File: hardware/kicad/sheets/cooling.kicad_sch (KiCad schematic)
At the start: 22 parts, among them J10 ALPHACOOL ES FLOW (3-pin), J11 ALPHACOOL ES NTC 10k, J8 FAN (4-pin PWM), J9 PUMP (4-pin PWM), U21 EMC2303-x-KP

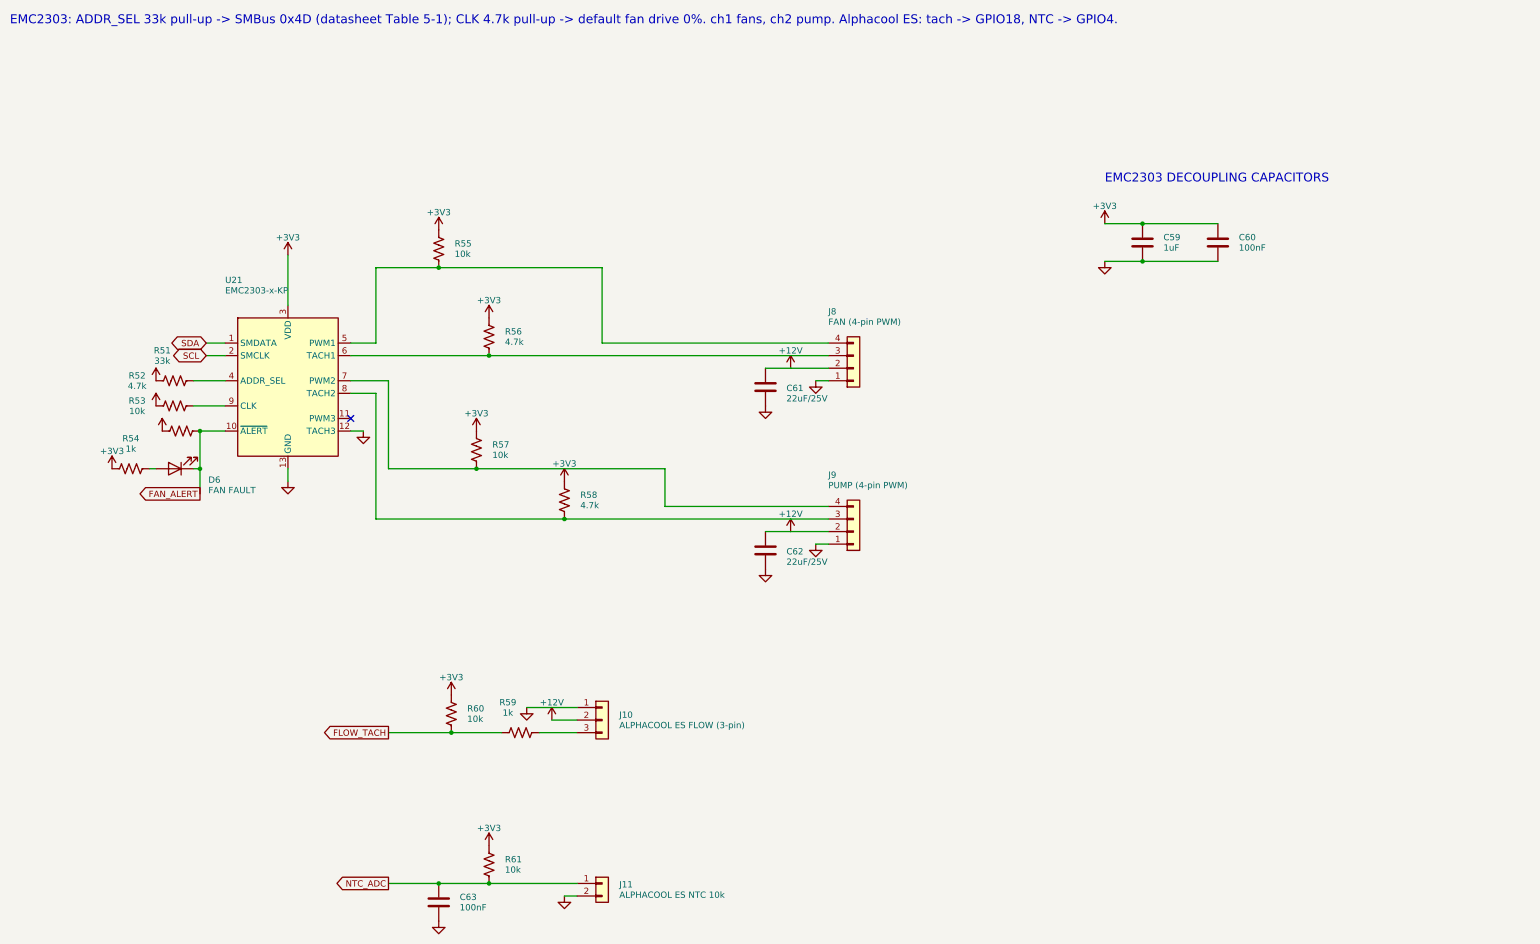
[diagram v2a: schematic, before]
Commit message: Fixing the UUID issues
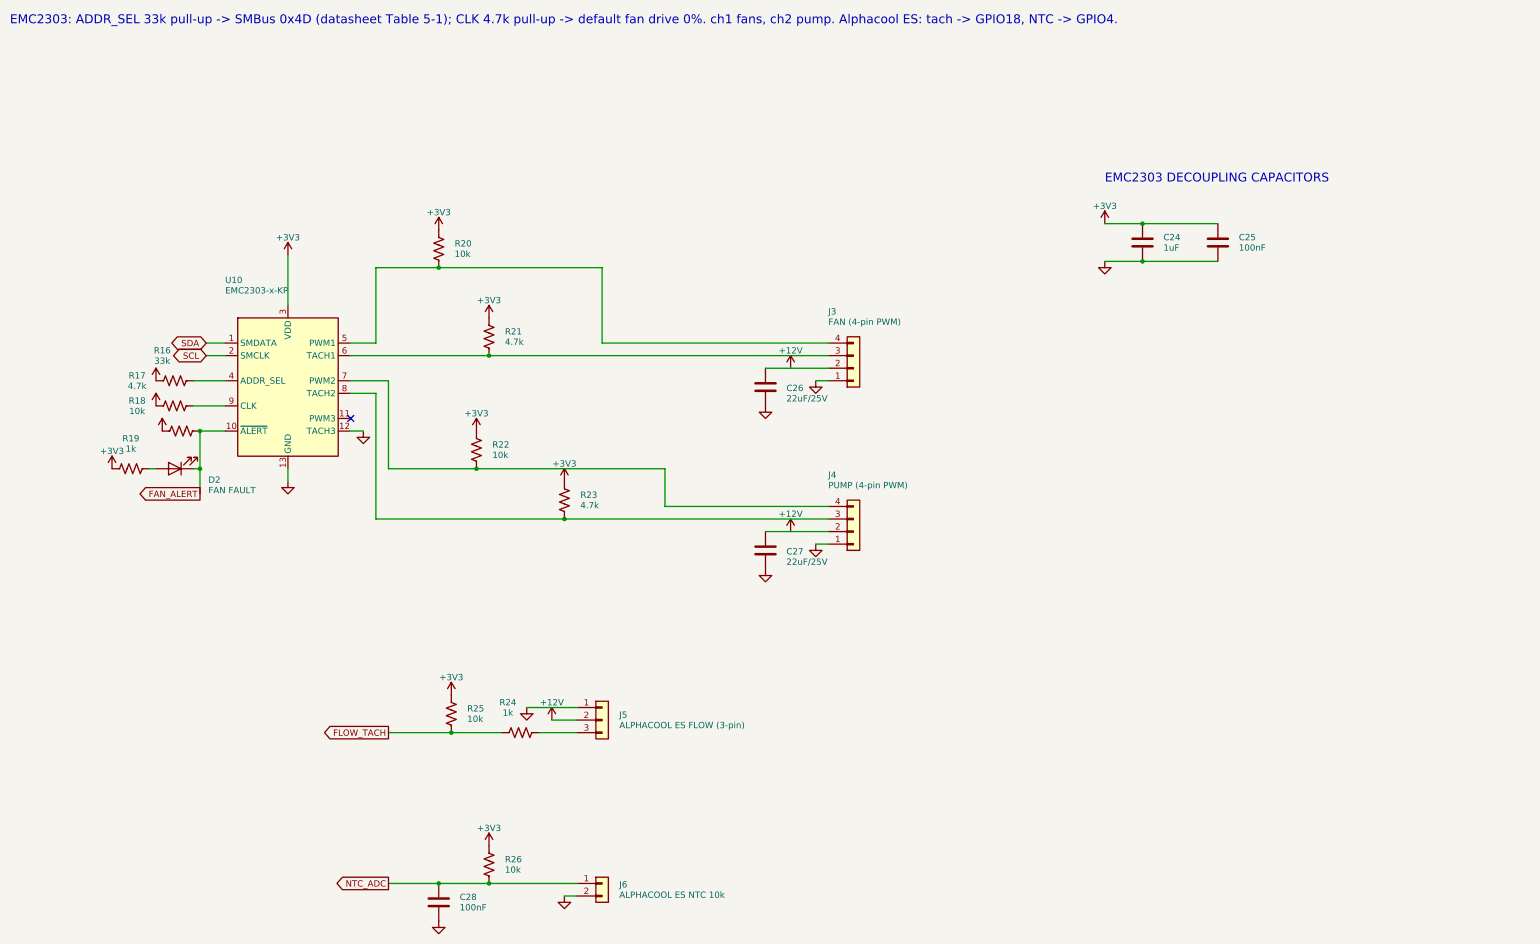
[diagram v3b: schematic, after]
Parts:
- removed C59: 1uF, Capacitor_SMD:C_0805_2012Metric, symbol Device:C
- removed C60, C63: 100nF, Capacitor_SMD:C_0603_1608Metric, symbol Device:C
- removed C61, C62: 22uF/25V, Capacitor_SMD:C_1210_3225Metric, symbol Device:C
- removed D6: FAN FAULT, LED_SMD:LED_0603_1608Metric, symbol Device:LED
- removed J10: ALPHACOOL ES FLOW (3-pin), Connector_Molex:Molex_KK-254_AE-6410-03A_1x03_P2.54mm_Vertical, symbol Connector_Generic:Conn_01x03
- removed J11: ALPHACOOL ES NTC 10k, Connector_JST:JST_XH_B2B-XH-A_1x02_P2.50mm_Vertical, symbol Connector_Generic:Conn_01x02
- removed J8: FAN (4-pin PWM), Connector_Molex:Molex_KK-254_AE-6410-04A_1x04_P2.54mm_Vertical, symbol Connector_Generic:Conn_01x04
- removed J9: PUMP (4-pin PWM), Connector_Molex:Molex_KK-254_AE-6410-04A_1x04_P2.54mm_Vertical, symbol Connector_Generic:Conn_01x04
- removed R51: 33k, Resistor_SMD:R_0603_1608Metric, symbol Device:R_US
- removed R52, R56, R58: 4.7k, Resistor_SMD:R_0603_1608Metric, symbol Device:R_US
- removed R53, R55, R57, R60, R61: 10k, Resistor_SMD:R_0603_1608Metric, symbol Device:R_US
- removed R54, R59: 1k, Resistor_SMD:R_0603_1608Metric, symbol Device:R_US
- removed U21: EMC2303-x-KP, Package_DFN_QFN:VQFN-12-1EP_4x4mm_P0.8mm_EP2.1x2.1mm_ThermalVias, symbol Driver_Motor:EMC2303-x-KP
- added C24: 1uF, Capacitor_SMD:C_0805_2012Metric, symbol Device:C
- added C25, C28: 100nF, Capacitor_SMD:C_0603_1608Metric, symbol Device:C
- added C26, C27: 22uF/25V, Capacitor_SMD:C_1210_3225Metric, symbol Device:C
- added D2: FAN FAULT, LED_SMD:LED_0603_1608Metric, symbol Device:LED
- added J3: FAN (4-pin PWM), Connector_Molex:Molex_KK-254_AE-6410-04A_1x04_P2.54mm_Vertical, symbol Connector_Generic:Conn_01x04
- added J4: PUMP (4-pin PWM), Connector_Molex:Molex_KK-254_AE-6410-04A_1x04_P2.54mm_Vertical, symbol Connector_Generic:Conn_01x04
- added J5: ALPHACOOL ES FLOW (3-pin), Connector_Molex:Molex_KK-254_AE-6410-03A_1x03_P2.54mm_Vertical, symbol Connector_Generic:Conn_01x03
- added J6: ALPHACOOL ES NTC 10k, Connector_JST:JST_XH_B2B-XH-A_1x02_P2.50mm_Vertical, symbol Connector_Generic:Conn_01x02
- added R16: 33k, Resistor_SMD:R_0603_1608Metric, symbol Device:R_US
- added R17, R21, R23: 4.7k, Resistor_SMD:R_0603_1608Metric, symbol Device:R_US
- added R18, R20, R22, R25, R26: 10k, Resistor_SMD:R_0603_1608Metric, symbol Device:R_US
- added R19, R24: 1k, Resistor_SMD:R_0603_1608Metric, symbol Device:R_US
- added U10: EMC2303-x-KP, Package_DFN_QFN:VQFN-12-1EP_4x4mm_P0.8mm_EP2.1x2.1mm_ThermalVias, symbol Driver_Motor:EMC2303-x-KP
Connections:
- net +12V: now also C26.1, C27.1, J3.2 (Pin_2), J4.2 (Pin_2), J5.2 (Pin_2)
- net +3V3: now also C24.1, C25.1, R16.1, R17.1, R18.1, R19.1, R20.1, R21.1, R22.1, R23.1, R25.1, R26.1, U10.3 (VDD)
- net FAN_ALERT: now also D2.1 (K), R18.2, U10.10 (~{ALERT})
- net FLOW_TACH: now also R24.1, R25.2
- net GND: now also C24.2, C25.2, C26.2, C27.2, C28.2, J3.1 (Pin_1), J4.1 (Pin_1), J5.1 (Pin_1), J6.2 (Pin_2), U10.12 (TACH3), U10.13 (GND)
- net NTC_ADC: now also C28.1, J6.1 (Pin_1), R26.2
- net SCL: now also U10.2 (SMCLK)
- net SDA: now also U10.1 (SMDATA)
- new net: J5.3 (Pin_3), R24.2
- new net: J3.4 (Pin_4), R20.2, U10.5 (PWM1)
- new net: D2.2 (A), R19.2
- new net: R16.2, U10.4 (ADDR_SEL)
- new net: J3.3 (Pin_3), R21.2, U10.6 (TACH1)
- new net: J4.4 (Pin_4), R22.2, U10.7 (PWM2)
- new net: J4.3 (Pin_3), R23.2, U10.8 (TACH2)
- new net: R17.2, U10.9 (CLK)
